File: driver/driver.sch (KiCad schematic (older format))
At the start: 46 parts

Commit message: Driver schematic progress
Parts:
- added C? (x7): 100n, symbol Device:C_Small
- added C? (x2): 12p, symbol Device:C_Small
- added C? (x2): 1u, symbol Device:C_Small
- added C?: 100u, symbol Device:CP_Small
- added C?: 22u, symbol Device:CP_Small
- added C?: 10u, symbol Device:C_Small
- added D? (x4): cyan, symbol Device:LED_Small_ALT
- added D? (x4): pink, symbol Device:LED_Small_ALT
- added J?: USB_B_Micro, symbol Connector:USB_B_Micro
- added J?: Conn_01x04, symbol Connector_Generic:Conn_01x04
- added J?: CH340E module, symbol Connector_Generic:Conn_01x06
- added J?: 1602 I2C LCD, symbol Connector_Generic:Conn_01x04
- added R? (x2): 10k, symbol Device:R_Small
- added R? (x2): 22, symbol Device:R_Small
- added R? (x5): 1k5, symbol Device:R_Small
- added R?: 680, symbol Device:R_Small
- added R? (x2): 390, symbol Device:R_Small
- added R?: 720, symbol Device:R_Small
- added R?: 10R .5W, symbol Device:R_Small
- added R? (x8): 150, symbol Device:R_Small
- added SW? (x2): SW_Push, symbol Switch:SW_Push
- added U? (x2): PC817, Package_DIP:DIP-4_W7.62mm, symbol Isolator:PC817
- added U?: AMS1117-5.0, Package_TO_SOT_SMD:SOT-223-3_TabPin2, symbol Regulator_Linear:AMS1117-3.3
- added U?: MCP9804_MSOP, Package_SO:MSOP-8_3x3mm_P0.65mm, symbol Sensor_Temperature:MCP9804_MSOP
- added Y?: 8MHz, symbol Device:Crystal_GND24
- J?: value Conn_01x02 -> PWR_IN
- J?: value Conn_01x02 -> BUS_OUT
- Q? (x4): value IRF7480M -> TPHR6503PL
- R?: value 5mR 1W -> 5mR 1W 2512
- R?: value 75k -> 100k
- R?: value 3.0k -> 3k3
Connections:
- net labels added: +3.3V, +5V, +VSW, DRV_A, DRV_B, ISO_5V, ISO_GND, LED0, LED1, LED2, LED3, LED4, LED5, LED6, LED7, SCL_INA, SCL_LCD, SDA_INA, SDA_LCD, SW0, SW1, UART_RX, UART_TX, USB_DM, USB_DP
- net labels removed: +15V, AH, AL, BH, BL
- wire segments 190 -> 392
- no-connect marks 0 -> 3
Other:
- note added: "18V"
- note added: "3V3"
- note added: "3V3 current mon I2C bus"
- note added: "5V"
- note added: "5V LCD I2C bus"
- note added: "DTR"
- note added: "GND"
- note added: "I2C addr=100'0000"
- note added: "I2C addr=100'1000"
- note added: "RXD"
- note added: "TXD"
- moved on the sheet: C?, D?, L?, R?, U?

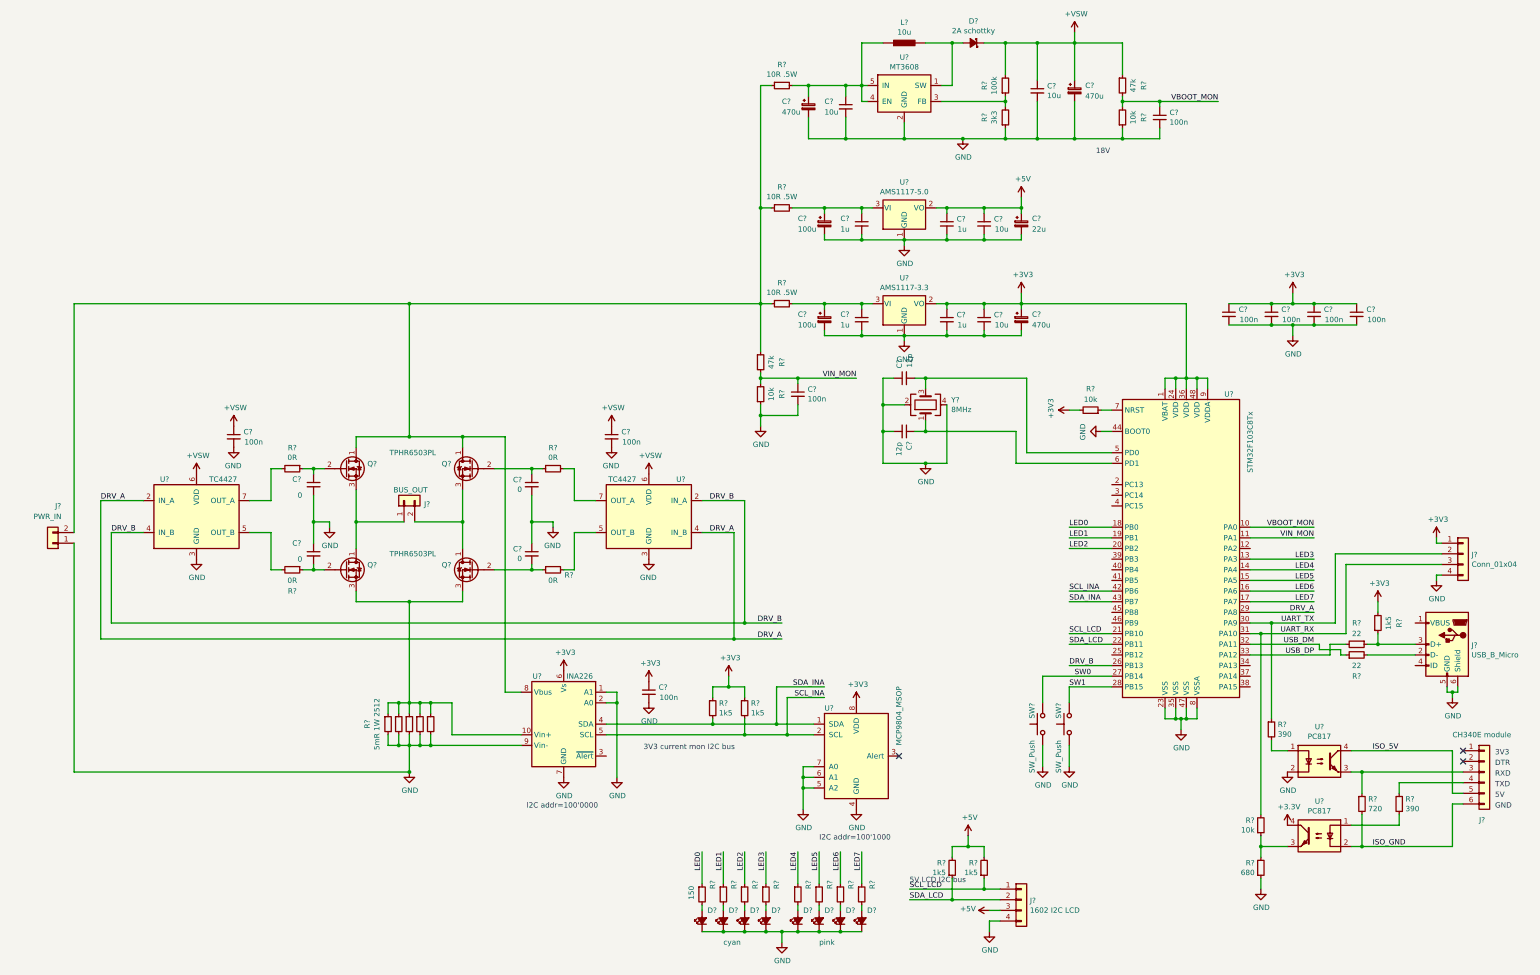
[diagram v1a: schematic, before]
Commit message: driver: Initial layout
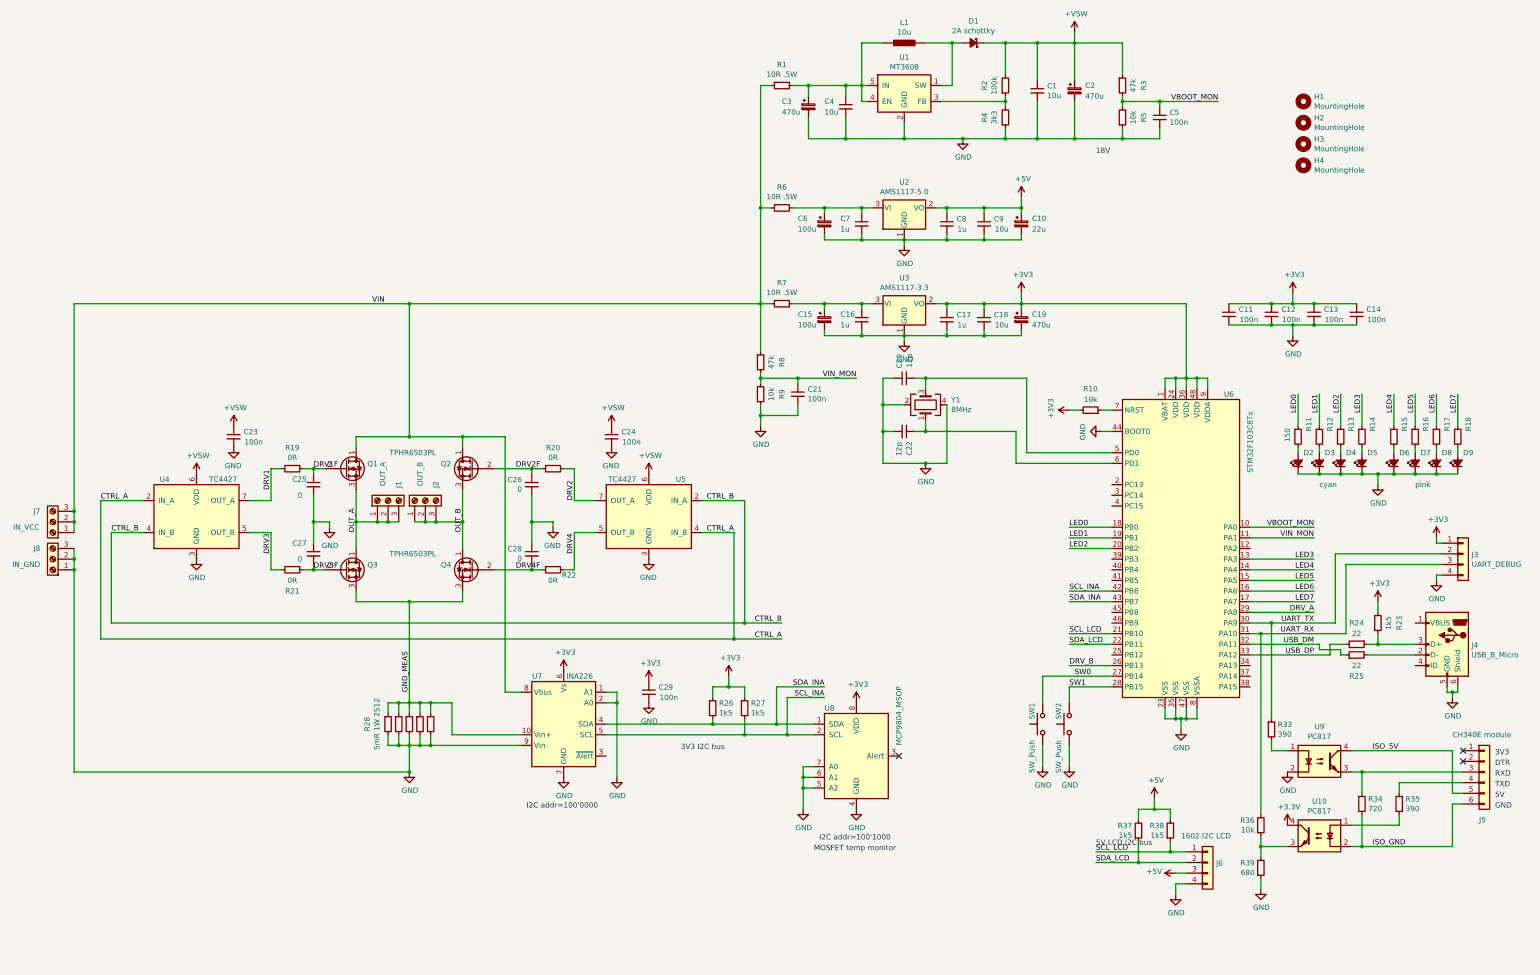
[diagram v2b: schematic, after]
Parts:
- removed J?: PWR_IN, symbol Connector_Generic:Conn_01x02
- removed J?: BUS_OUT, symbol Connector_Generic:Conn_01x02
- added H1, H2, H3, H4: MountingHole, MountingHole:MountingHole_3.2mm_M3, symbol Mechanical:MountingHole
- added J1: OUT_A, TerminalBlock_Phoenix:TerminalBlock_Phoenix_MKDS-1,5-3-5.08_1x03_P5.08mm_Horizontal, symbol Connector:Screw_Terminal_01x03
- added J2: OUT_B, TerminalBlock_Phoenix:TerminalBlock_Phoenix_MKDS-1,5-3-5.08_1x03_P5.08mm_Horizontal, symbol Connector:Screw_Terminal_01x03
- added J7: IN_VCC, TerminalBlock_Phoenix:TerminalBlock_Phoenix_MKDS-1,5-3-5.08_1x03_P5.08mm_Horizontal, symbol Connector:Screw_Terminal_01x03
- added J8: IN_GND, TerminalBlock_Phoenix:TerminalBlock_Phoenix_MKDS-1,5-3-5.08_1x03_P5.08mm_Horizontal, symbol Connector:Screw_Terminal_01x03
- C1, C11, C12, C13, C14, C15, C16, C17, C18, C20, C21, C22, C23, C24, C25, C26, C27, C28, C29, C4, C5, C7, C8, C9: renamed from C?; footprint (none) -> Capacitors_SMD:C_0603_HandSoldering
- C10: renamed from C?; footprint (none) -> Capacitor_THT:CP_Radial_D5.0mm_P2.00mm
- C19, C2, C3, C6: renamed from C?; footprint (none) -> Capacitor_THT:CP_Radial_D12.5mm_P5.00mm
- D1: renamed from D?; footprint (none) -> Diode_SMD:D_SMB_Handsoldering
- D2, D3, D4, D5, D6, D7, D8, D9: renamed from D?; footprint (none) -> LED_SMD:LED_PLCC_2835_Handsoldering
- J3: renamed from J?; value Conn_01x04 -> UART_DEBUG; footprint (none) -> Pin_Headers:Pin_Header_Straight_1x04_Pitch2.54mm
- J4: renamed from J?; footprint (none) -> footprints:microusb_ali_dovetail
- J5: renamed from J?; footprint (none) -> Pin_Headers:Pin_Header_Straight_1x06_Pitch2.54mm
- J6: renamed from J?; footprint (none) -> Connectors_Molex:Molex_KK-6410-04_04x2.54mm_Straight
- L1: renamed from L?; footprint (none) -> Inductor_SMD:L_Taiyo-Yuden_NR-50xx_HandSoldering
- Q1, Q2, Q3, Q4: renamed from Q?; footprint Package_DirectFET:DirectFET_ME -> footprints:Toshiba SOP Advance
- R1, R10, R11, R12, R13, R14, R15, R16, R17, R18, R19, R2, R20, R21, R22, R23, R24, R25, R26, R27, R3, R33, R34, R35, R36, R37, R38, R39, R4, R5, R8, R9: renamed from R?; footprint (none) -> Resistor_SMD:R_0603_1608Metric_Pad1.05x0.95mm_HandSolder
- R28, R29, R30, R31, R32: renamed from R?; footprint (none) -> Resistor_SMD:R_2512_6332Metric_Pad1.52x3.35mm_HandSolder
- R6, R7: renamed from R?; footprint (none) -> Resistor_SMD:R_1206_3216Metric_Pad1.42x1.75mm_HandSolder
- SW1, SW2: renamed from SW?; footprint (none) -> Button_Switch_THT:SW_PUSH_6mm
- U1: renamed from U?; footprint (none) -> Package_TO_SOT_SMD:SOT-23-6_Handsoldering
- U4, U5: renamed from U?; footprint (none) -> Package_SO:SOIC-8_3.9x4.9mm_P1.27mm
- U8: renamed from U?; footprint Package_SO:MSOP-8_3x3mm_P0.65mm -> Package_SO:SOIC-8_3.9x4.9mm_P1.27mm
- Y1: renamed from Y?; footprint (none) -> Crystal:Crystal_SMD_3225-4Pin_3.2x2.5mm_HandSoldering
- gave numbers to parts that had none: 6
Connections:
- net DRV_A: no longer U4.2 (IN_A), U5.4 (IN_B)
- net DRV_B: no longer U4.4 (IN_B), U5.2 (IN_A)
- net GND: now also J8.1 (Pin_1), J8.2 (Pin_2), J8.3 (Pin_3)
- net GND_MEAS: now reaches Q3.3 (S), Q4.3 (S), R28.1, R29.1, R30.1, R31.1, R32.1, U7.10 (Vin+)
- net VIN: now reaches Q1.1 (D), Q2.1 (D), R1.1, R6.1, R7.1, R8.1, U7.8 (Vbus)
- net VIN: now also J7.1 (Pin_1), J7.2 (Pin_2), J7.3 (Pin_3)
- net OUT_A: now reaches Q1.3 (S), Q3.1 (D)
- net OUT_A: now also J1.1 (Pin_1), J1.2 (Pin_2), J1.3 (Pin_3)
- net DRV3F: now reaches C27.2, Q3.2 (G), R21.1
- net DRV1F: now reaches C25.1, Q1.2 (G), R19.1
- net DRV2F: now reaches C26.1, Q2.2 (G), R20.1
- net OUT_B: now reaches Q2.3 (S), Q4.1 (D)
- net OUT_B: now also J2.1 (Pin_1), J2.2 (Pin_2), J2.3 (Pin_3)
- net DRV4F: now reaches C28.2, Q4.2 (G), R22.1
- net DRV1: now reaches R19.2, U4.7 (OUT_A)
- net DRV3: now reaches R21.2, U4.5 (OUT_B)
- net DRV2: now reaches R20.2, U5.7 (OUT_A)
- net DRV4: now reaches R22.2, U5.5 (OUT_B)
- new net CTRL_A: U4.2 (IN_A), U5.4 (IN_B)
- new net CTRL_B: U4.4 (IN_B), U5.2 (IN_A)
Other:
- note added: "3V3 I2C bus"
- note added: "MOSFET temp monitor"
- note removed: "3V3 current mon I2C bus"
- moved on the sheet: D2, D3, D4, D5, D6, D7, D8, D9, J6, R11, R12, R13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
